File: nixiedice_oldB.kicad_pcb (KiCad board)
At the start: 2 copper layers, 127 x 63.5 mm, 51 parts, among them CON1 BARREL_JACK, M1 1pin, M2 1pin, M3 1pin, M4 1pin, P1 USB_OTG, P2 USB_A, P3 ARDUINO PRO MICRO, P8 CONN_01X04, Q1 MPSA42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

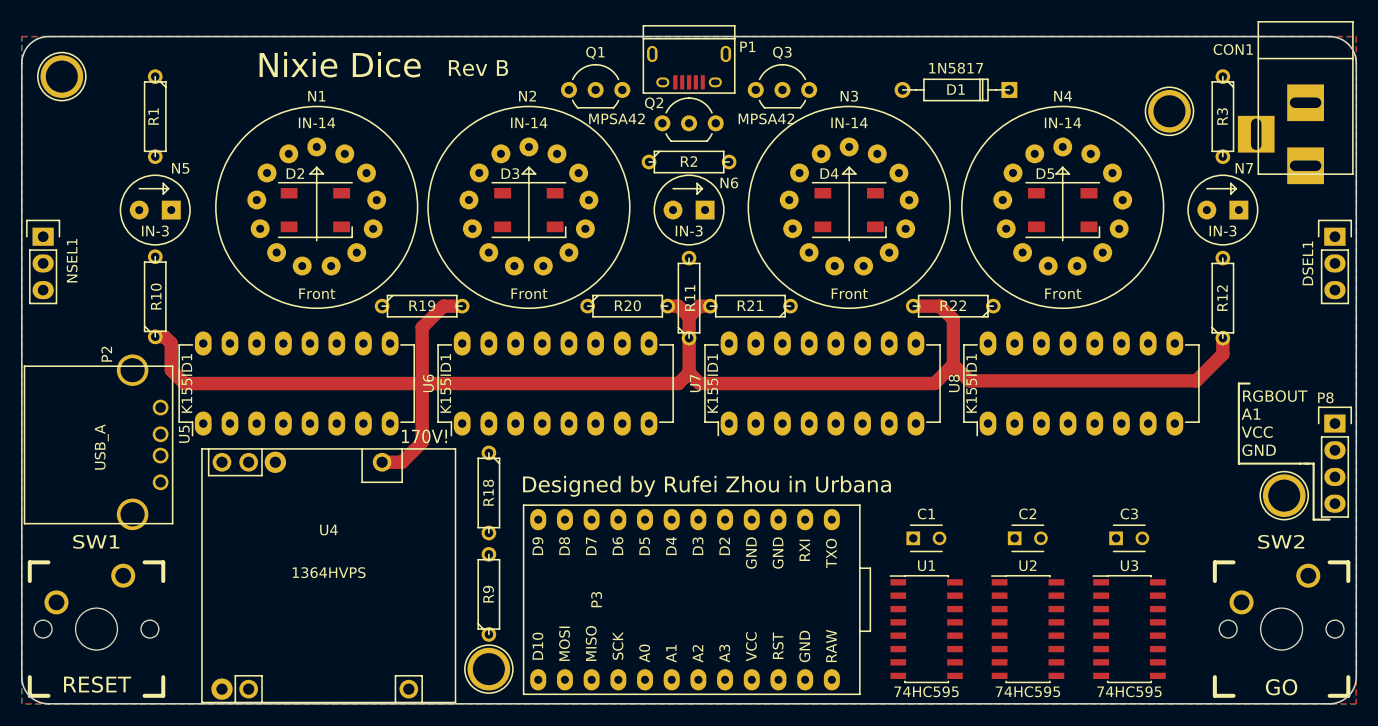
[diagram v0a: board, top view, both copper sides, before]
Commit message: fix IN-14 footprint being upside down
ussr datasheet is backwards af
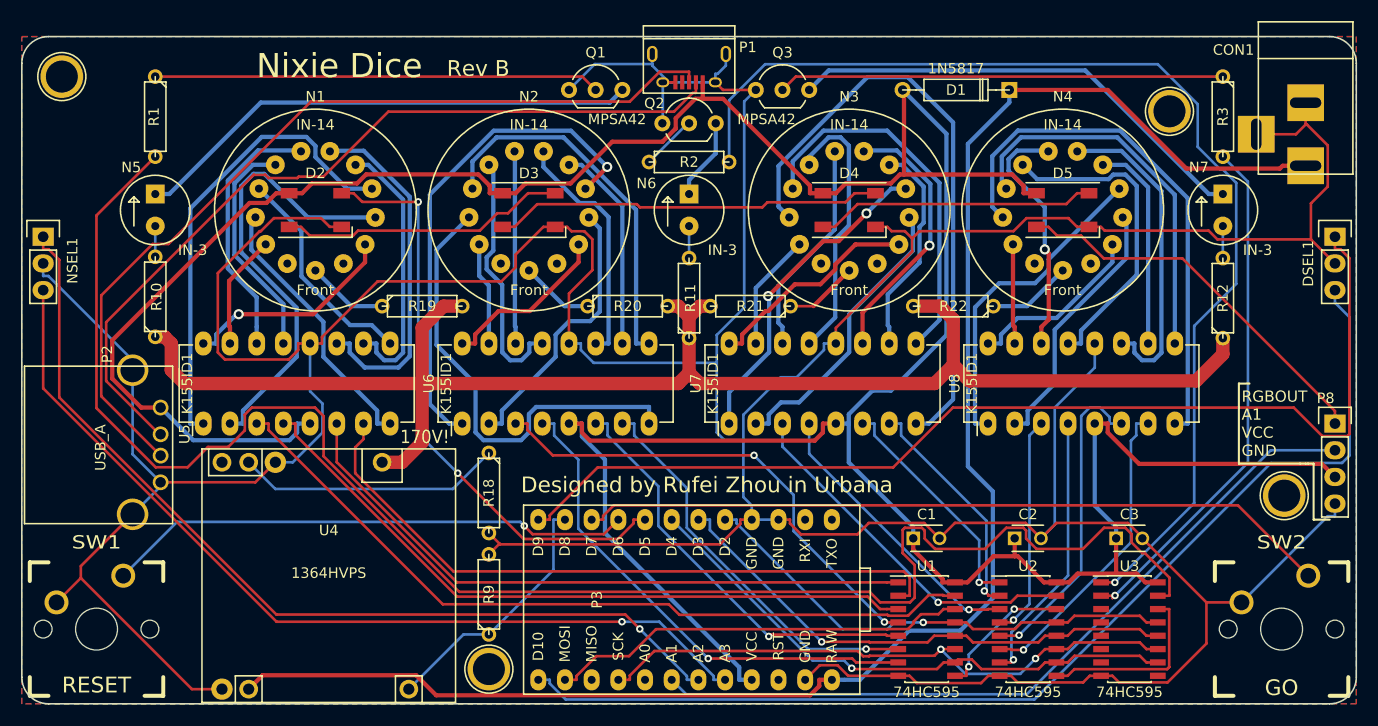
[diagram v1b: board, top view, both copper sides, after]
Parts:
- moved N1 0.28 mm to (27.9, 16.5)
- moved N2 0.25 mm to (48.3, 16.5)
- moved N3 0.25 mm to (78.7, 16.5)
- moved N4 0.25 mm to (99.1, 16.5)
- turned N5 to 180 degrees
- turned N6 to 180 degrees
- turned N7 to 180 degrees
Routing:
- net GND: track 0.00 -> 506.6 mm
- net VCC: track 0.00 -> 326.4 mm
- net Net-(R1-Pad2): track 0.00 -> 161.6 mm
- net /RAW: track 0.00 -> 158.7 mm
- net Net-(R2-Pad2): track 0.00 -> 106.7 mm, vias 0 -> 1
- net /D10: track 0.00 -> 104.1 mm
- net /D9: track 0.00 -> 102.7 mm
- net /A2: track 0.00 -> 88.4 mm, vias 0 -> 1
- net /A3: track 0.00 -> 85.9 mm, vias 0 -> 1
- net /D+: track 0.00 -> 83.3 mm
- net /D-: track 0.00 -> 79.3 mm
- net /T1INA: track 0.00 -> 75.2 mm
- net /A1: track 0.00 -> 73.3 mm
- net /BTN_GO: track 0.00 -> 71.7 mm
- net /T1IND: track 0.00 -> 66.4 mm
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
